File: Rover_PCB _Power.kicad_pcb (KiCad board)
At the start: 2 copper layers, 100 x 100 mm, 65 parts, among them J10 LED_U_RGY, J11 CAN_S1, J12 CAN_S2, J13 CAN_S3, J14 CAN_S4, J15 CAN_S5, J16 CAN_S6, J17 CAN7, J18 CAN8, J2 Brushed_Motor1, J20 Servo1, J21 Servo2, J22 Servo3, J23 Servo4, J24 Servo5, J25 Servo6, J26 Servo7, J27 Servo8, J28 UART1, J29 UART2, J3 Brushed_Motor2, J30 3.3V, J31 5V, J32 12V, J33 24V, J34 48V, J36 Safety_Button, J37 STLINK, J39 Load_Cell1, J4 LED_R_LR, J40 Load_Cell2, J41 Load_Cell3, J42 Load_Cell4, J48 ATX, J49 Conn_01x30_Socket, J5 LED_R_LR, J50 FFC, J51 NTC1, J52 NTC2, J53 NTC3, J54 NTC4, J55 XT60_24V_OUT, J56 XT60_24V_OUT, J57 XT60_24V_OUT, J58 XT60_24V_OUT, J59 XT30_24V_OUT, J6 LED_R_RR, J60 XT30_24V_OUT, J61 XT30_24V_OUT, J62 XT30_24V_OUT, J63 XT60_48V_OUT, J64 XT60_48V_OUT, J65 XT60_12V_OUT, J66 XT60_12V_OUT, J67 XT30_48V_OUT, J68 XT30_48V_OUT, J69 XT30_12V_OUT, J7 LED_R_RL, J70 XT30_12V_OUT, J71 FFC, J73 BAT1, J74 BAT_TOTAL, J8 LED_F_R, J9 LED_F_L

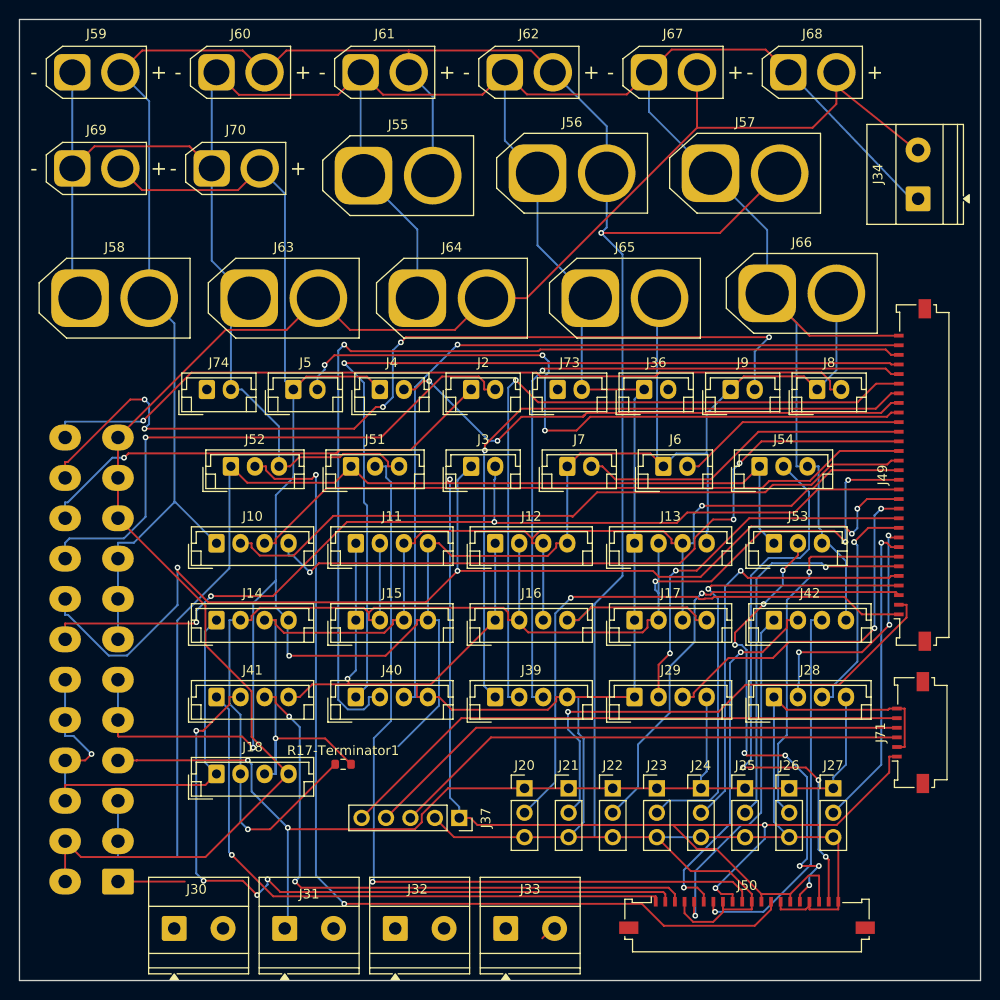
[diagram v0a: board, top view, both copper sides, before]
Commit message: Aktualizacja plytki zasilania (Power), uaktualnienie README.md o szczegoly klas netow i grubosci sciezek na obu plytkach
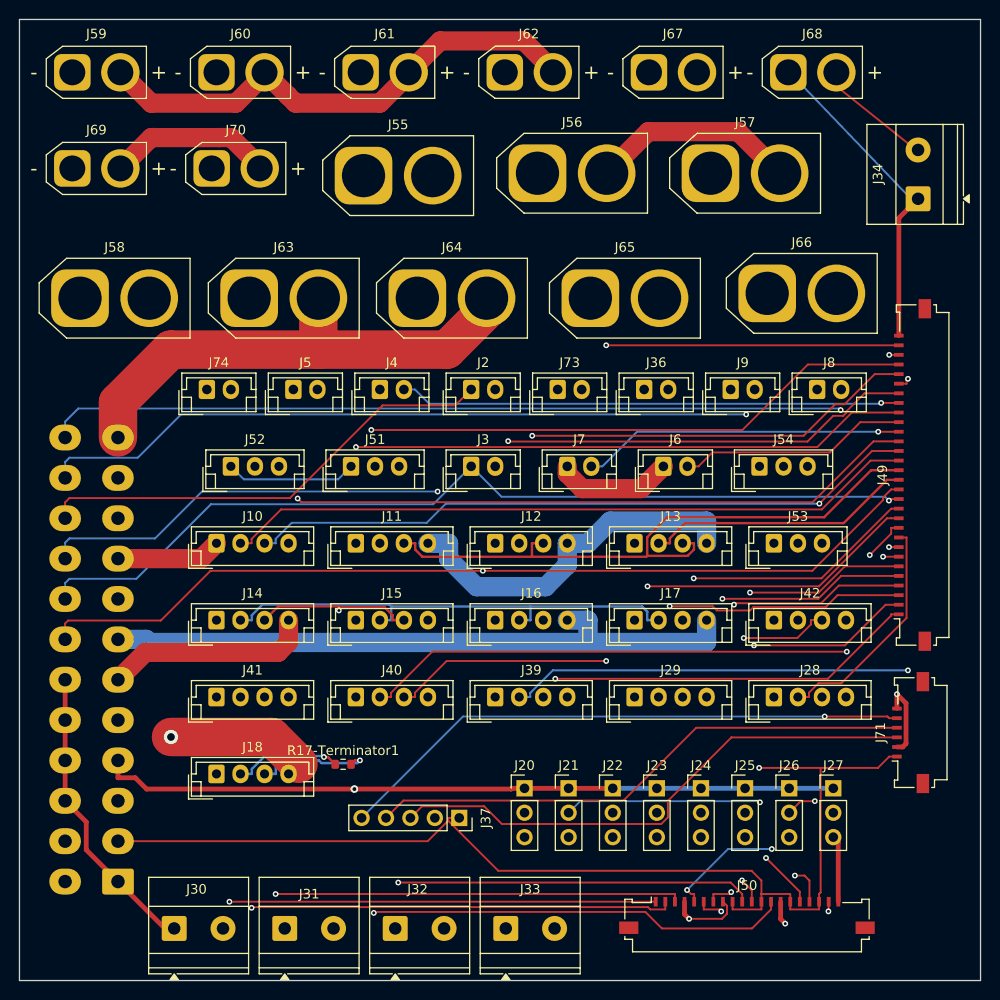
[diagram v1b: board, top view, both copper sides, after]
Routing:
- net /GND: track 616.9 -> 77.9 mm, vias 2 -> 5
- net /+12V: track 255.2 -> 281.1 mm, vias 2 -> 0
- net /OUTA2: track 116.2 -> 95.0 mm, vias 4 -> 1
- net /+24V: track 260.8 -> 280.6 mm, vias 1 -> 0
- net /INA1-: track 101.3 -> 84.5 mm, vias 1 -> 2
- net /PC6: track 93.9 -> 77.5 mm, vias 5 -> 1
- net /+3.3V: track 243.4 -> 227.3 mm, vias 3 -> 1
- net /CANH: track 144.8 -> 131.9 mm, vias 4 -> 1
- net /+48V: track 179.2 -> 191.7 mm, vias 0 -> 1
- net /PC3: track 58.7 -> 49.9 mm, vias 3 -> 1
- net /PC2: track 49.2 -> 41.6 mm, vias 8 -> 1
- net /AVDD1: track 94.0 -> 86.4 mm
- net /INA2-: track 73.5 -> 67.1 mm, vias 4 -> 1
- net /OUTB2: track 100.8 -> 106.4 mm, vias 3 -> 1
- net /PE9: track 59.5 -> 53.9 mm
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- added copper zone on In2.Cu, net /GND
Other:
- copper layers 2 -> 4
